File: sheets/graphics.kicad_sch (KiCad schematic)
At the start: 23 parts, among them J2 CUT DOG, SW1 RESET SWITCH, U13 NEO-B1, U14 PST518B, U15 74LS244, U16 TC531000AP, U17 uPD43256AGU-12L, U18 uPD43256AGU-12L, U19 CXK5864P-35, U20 CXK5864P-35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

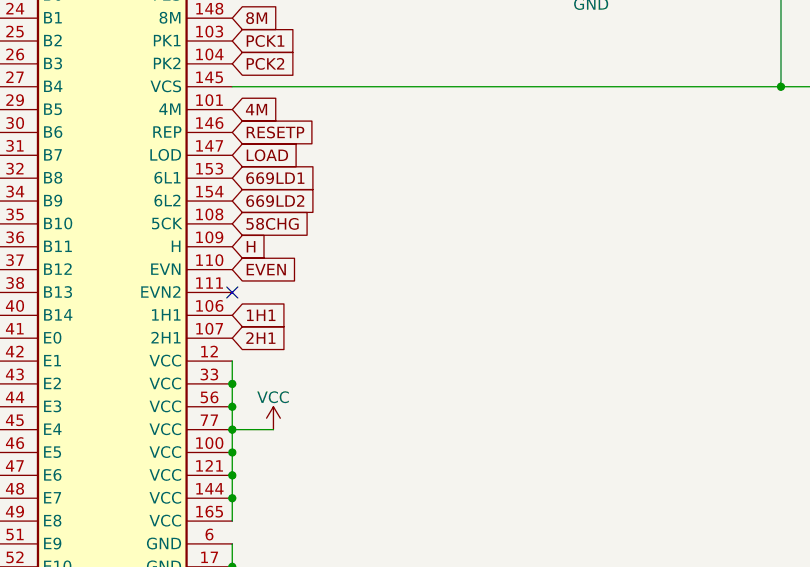
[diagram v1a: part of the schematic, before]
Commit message: Added missing J3 and J4 for EVEN pin from LSPC2. Missing from original schematics Fixed RA1 being wrong way U38 pins 12/13 to VCC
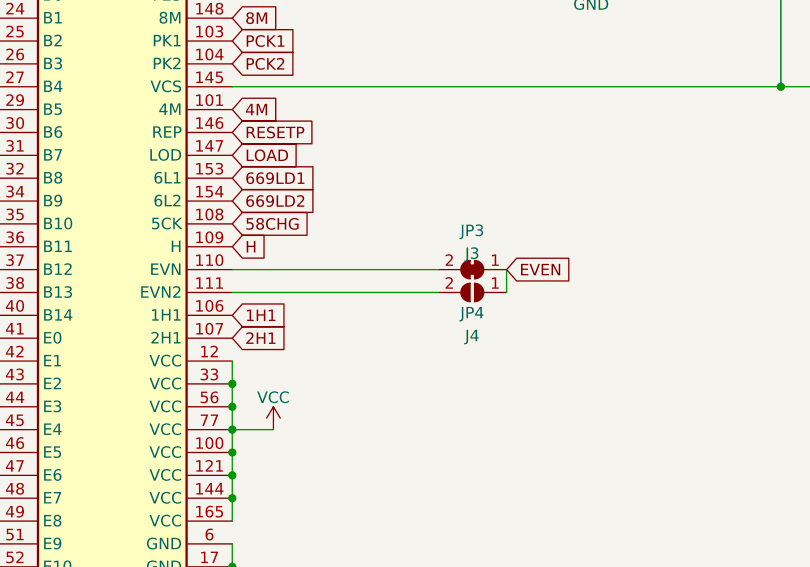
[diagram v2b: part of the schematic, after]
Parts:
- added JP3: J3, symbol Jumper:SolderJumper_2_Bridged
- added JP4: J4, symbol Jumper:SolderJumper_2_Open
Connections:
- net EVEN: now also JP3.1 (A), JP4.1 (A); no longer U21.110 (EVN)
- net at U21.111 (EVN2): now also JP4.2 (B)
- new net: JP3.2 (B), U21.110 (EVN)
- no-connect marks 16 -> 15
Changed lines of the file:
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@@
   (no_connect (at 373.126 177.292))
   (no_connect (at 373.126 179.832))
-  (no_connect (at 182.372 135.636))
   (no_connect (at 155.702 237.236))
   (no_connect (at 347.726 146.812))
@@
     (stroke (width 0) (type default) (color 0 0 0 0))
   )
+  (wire (pts (xy 212.852 133.096) (xy 212.852 135.636))
+    (stroke (width 0) (type default) (color 0 0 0 0))
+  )
   (bus (pts (xy 85.344 140.716) (xy 85.344 143.256))
     (stroke (width 0) (type default) (color 0 0 0 0))
@@
     (stroke (width 0) (type default) (color 0 0 0 0))
   )
+  (wire (pts (xy 182.372 133.096) (xy 205.232 133.096))
+    (stroke (width 0) (type default) (color 0 0 0 0))
+  )
   (bus (pts (xy 192.278 72.136) (xy 192.278 69.596))
     (stroke (width 0) (type default) (color 0 0 0 0))
@@
     (stroke (width 0) (type default) (color 0 0 0 0))
   )
+  (wire (pts (xy 182.372 135.636) (xy 205.232 135.636))
+    (stroke (width 0) (type default) (color 0 0 0 0))
+  )
   (wire (pts (xy 329.184 174.752) (xy 347.726 174.752))
     (stroke (width 0) (type default) (color 0 0 0 0))
@@
     )
   )
-  (global_label "EVEN" (shape input) (at 182.372 133.096 0) (fields_autoplaced)
+  (global_label "EVEN" (shape input) (at 212.852 133.096 0) (fields_autoplaced)
     (effects (font (size 1.27 1.27)) (justify left))
-    (property "Intersheet References" "${INTERSHEET_REFS}" (id 0) (at 189.5022 133.0166 0)
+    (property "Intersheet References" "${INTERSHEET_REFS}" (id 0) (at 219.9822 133.0166 0)
       (effects (font (size 1.27 1.27)) (justify left) hide)
     )
@@
     (pin "1")
   )
+  (symbol (lib_id "Jumper:SolderJumper_2_Bridged") (at 209.042 133.096 180) (unit 1)
+    (in_bom yes) (on_board yes)
+    (property "Reference" "JP3" (id 0) (at 209.042 128.778 0))
+    (property "Value" "J3" (id 1) (at 209.042 131.318 0))
+    (property "Footprint" "" (id 2) (at 209.042 133.096 0)
+      (effects (font (size 1.27 1.27)) hide)
+    )
+    (property "Datasheet" "~" (id 3) (at 209.042 133.096 0)
+      (effects (font (size 1.27 1.27)) hide)
+    )
+    (pin "1")
+    (pin "2")
+  )
   (symbol (lib_id "Device:C_Small") (at 301.752 192.024 0) (unit 1)
     (in_bom yes) (on_board yes) (fields_autoplaced)
@@
     (pin "99")
   )
+  (symbol (lib_id "Jumper:SolderJumper_2_Open") (at 209.042 135.636 0) (mirror y) (unit 1)
+    (in_bom yes) (on_board yes)
+    (property "Reference" "JP4" (id 0) (at 209.042 137.922 0))
+    (property "Value" "J4" (id 1) (at 209.042 140.462 0))
+    (property "Footprint" "" (id 2) (at 209.042 135.636 0)
+      (effects (font (size 1.27 1.27)) hide)
+    )
+    (property "Datasheet" "~" (id 3) (at 209.042 135.636 0)
+      (effects (font (size 1.27 1.27)) hide)
+    )
+    (pin "1")
+    (pin "2")
+  )
   (symbol (lib_id "power:GND") (at 46.482 161.036 90) (unit 1)

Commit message: Added footprint to JP3 and JP4
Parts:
- JP3: footprint (none) -> Jumper:SolderJumper-2_P1.3mm_Closed_Pad1.0x1.5mm
- JP4: footprint (none) -> Jumper:SolderJumper-2_P1.3mm_Open_Pad1.0x1.5mm
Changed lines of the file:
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@@
     (property "Reference" "JP3" (id 0) (at 209.042 128.778 0))
     (property "Value" "J3" (id 1) (at 209.042 131.318 0))
-    (property "Footprint" "" (id 2) (at 209.042 133.096 0)
+    (property "Footprint" "Jumper:SolderJumper-2_P1.3mm_Closed_Pad1.0x1.5mm" (id 2) (at 209.042 133.096 0)
       (effects (font (size 1.27 1.27)) hide)
     )
@@
     (property "Reference" "JP4" (id 0) (at 209.042 137.922 0))
     (property "Value" "J4" (id 1) (at 209.042 140.462 0))
-    (property "Footprint" "" (id 2) (at 209.042 135.636 0)
-      (effects (font (size 1.27 1.27)) hide)
-    )
+    (property "Footprint" "Jumper:SolderJumper-2_P1.3mm_Open_Pad1.0x1.5mm" (id 2) (at 209.042 135.636 0)
+      (effects (font (size 1.27 1.27)) hide)
+    )

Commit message: Selected footprint that actually exists
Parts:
- JP3: footprint Jumper:SolderJumper-2_P1.3mm_Closed_Pad1.0x1.5mm -> Jumper:SolderJumper-2_P1.3mm_Bridged_Pad1.0x1.5mm
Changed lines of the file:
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@@
     (property "Reference" "JP3" (id 0) (at 209.042 128.778 0))
     (property "Value" "J3" (id 1) (at 209.042 131.318 0))
-    (property "Footprint" "Jumper:SolderJumper-2_P1.3mm_Closed_Pad1.0x1.5mm" (id 2) (at 209.042 133.096 0)
+    (property "Footprint" "Jumper:SolderJumper-2_P1.3mm_Bridged_Pad1.0x1.5mm" (id 2) (at 209.042 133.096 0)
       (effects (font (size 1.27 1.27)) hide)
     )
